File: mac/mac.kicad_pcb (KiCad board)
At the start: 2 copper layers, 70 x 45 mm, 87 parts, among them M3 Отверстие_М3

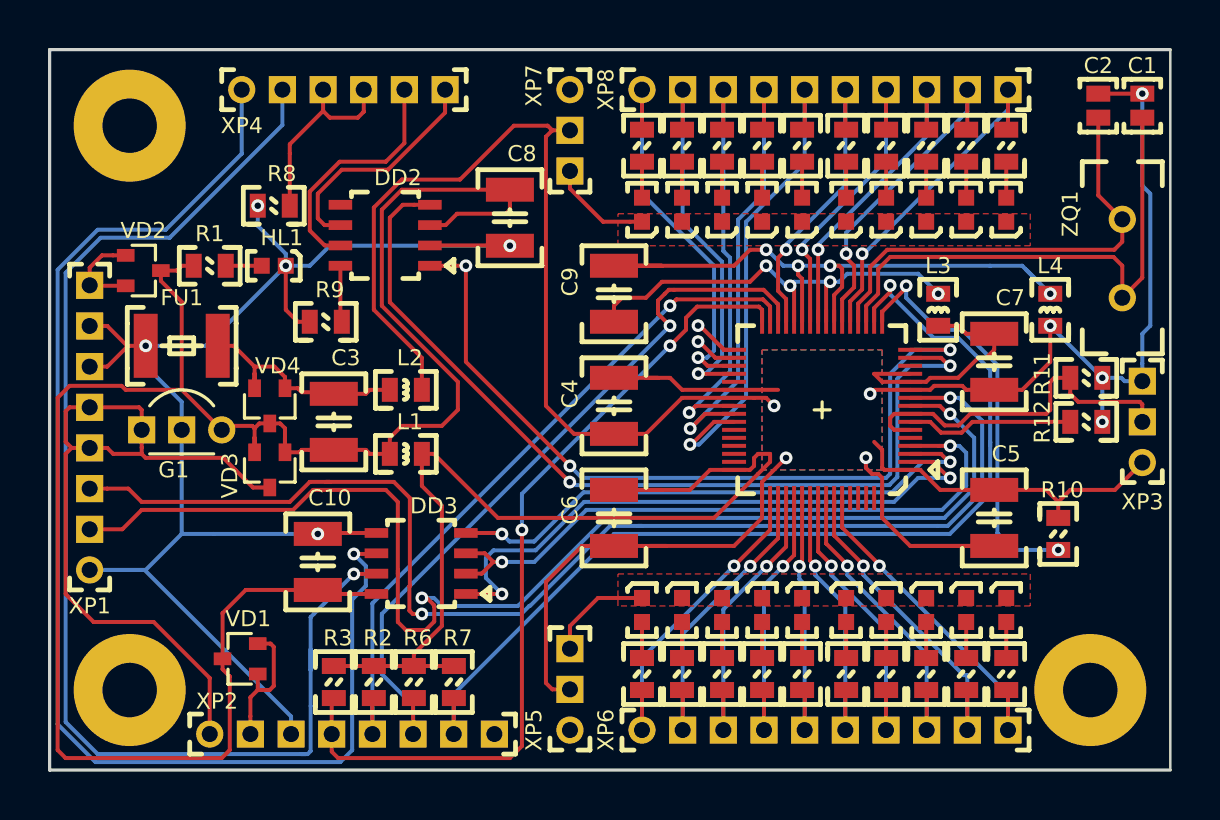
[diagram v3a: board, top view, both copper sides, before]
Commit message: причесывание
-изменен габарит: 72х47 мм
-добавлены заливки земли на обратной стороне
-переходные отверстия вынесены за пределы контактных площадок
-прототип рекламки шелкографией
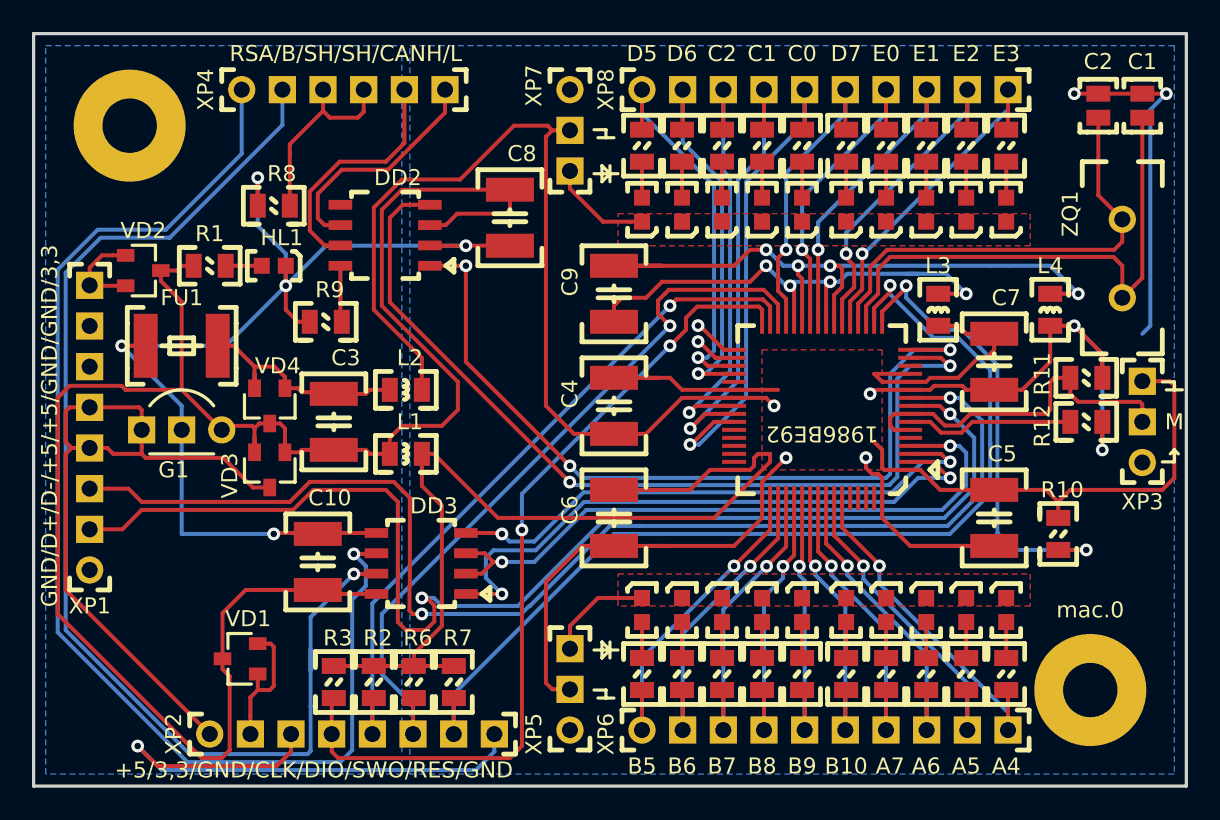
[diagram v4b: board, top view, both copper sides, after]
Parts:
- removed the M3 at (82.5, 97.5)
- moved G*** 4.80 mm to (113.5, 71.5)
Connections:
- XP2 pad 8: Net-(XP2-Pad8) -> /GND
- XP3 pad 1: /VCC_MC -> /GND_MC
- XP3 pad 3: /GND_MC -> /VCC_MC
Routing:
- net /GND: track 95.2 -> 105.9 mm, vias 5 -> 6
- net /VCC_MC: track 106.9 -> 116.3 mm
- net /GND_MC: track 151.8 -> 157.9 mm
- net /VCC: track 126.5 -> 121.5 mm
- net /A_VCC_MC: track 28.6 -> 32.8 mm
- net Net-(DD1-Pad17): track 25.8 -> 29.3 mm
- net /RS_B: track 79.0 -> 75.7 mm
- net /RS_A: track 81.7 -> 78.3 mm
- net /+4...30: track 47.5 -> 45.3 mm
- net /A_GND_MC: track 42.2 -> 44.3 mm
- added copper zone on B.Cu, net /GND
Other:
- board size 70 x 45 mm -> 72 x 47 mm
- board text added: "+5/3,3/GND/CLK/DIO/SWO/RES/GND"
- board text added: "- Разработка (PCB-design) - Опытное изготовление - Мелкосерийный монтаж печатных плат"
- board text added: "1986ВЕ92"
- board text added: "A4"
- board text added: "A5"
- board text added: "A6"
- board text added: "A7"
- board text added: "B10"
- board text added: "B5"
- board text added: "B6"
- board text added: "B7"
- board text added: "B8"
- board text added: "B9"
- board text added: "C0"
- board text added: "C1"
- board text added: "C2"
- board text added: "D5"
- board text added: "D6"
- board text added: "D7"
- board text added: "E0"
- board text added: "E1"
- board text added: "E2"
- board text added: "E3"
- board text added: "El.Nikitos@mail.ru +7(999)123-45-67 WhatsApp, Viber"
- board text added: "GND/D+/D-/+5/+5/GND/GND/3,3"
- board text added: "M"
- board text added: "RSA/B/SH/SH/CANH/L"

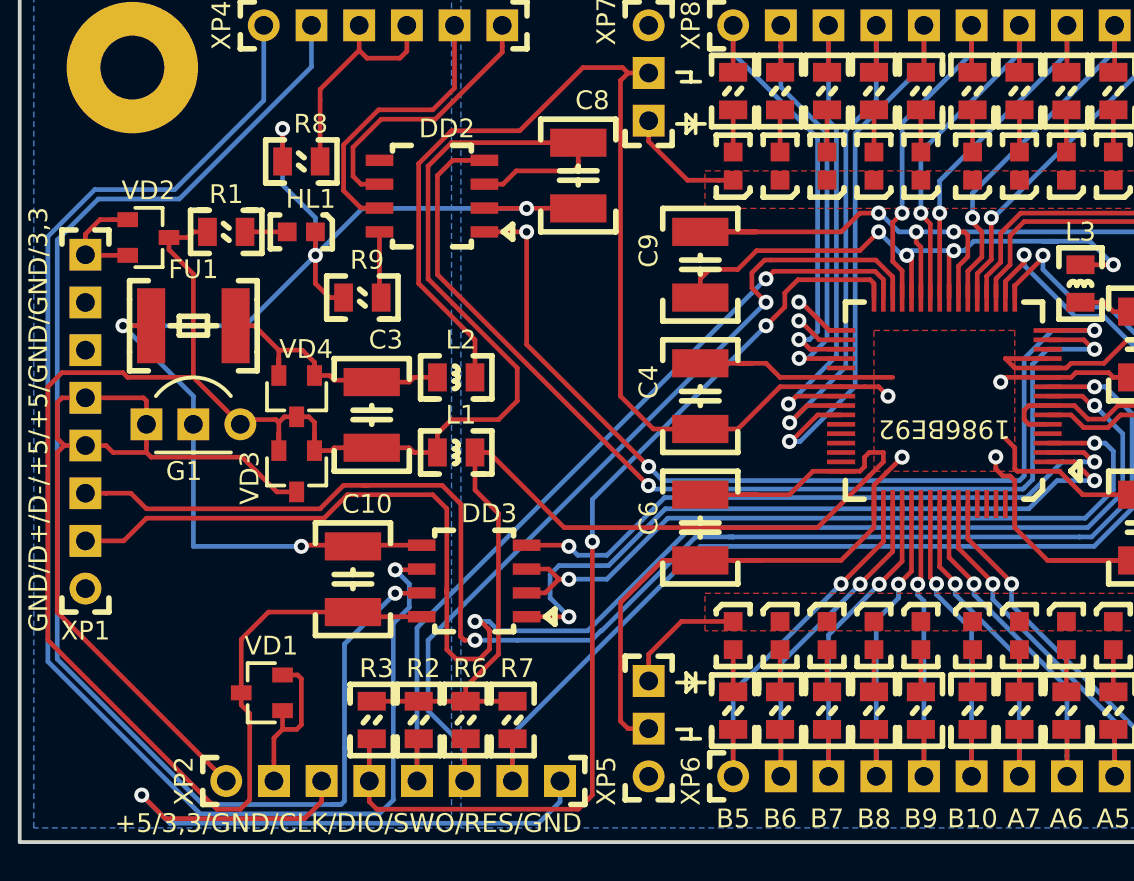
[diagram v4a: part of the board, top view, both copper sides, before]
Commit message: добавлен номер телефона, исправлено положение стабилизатора
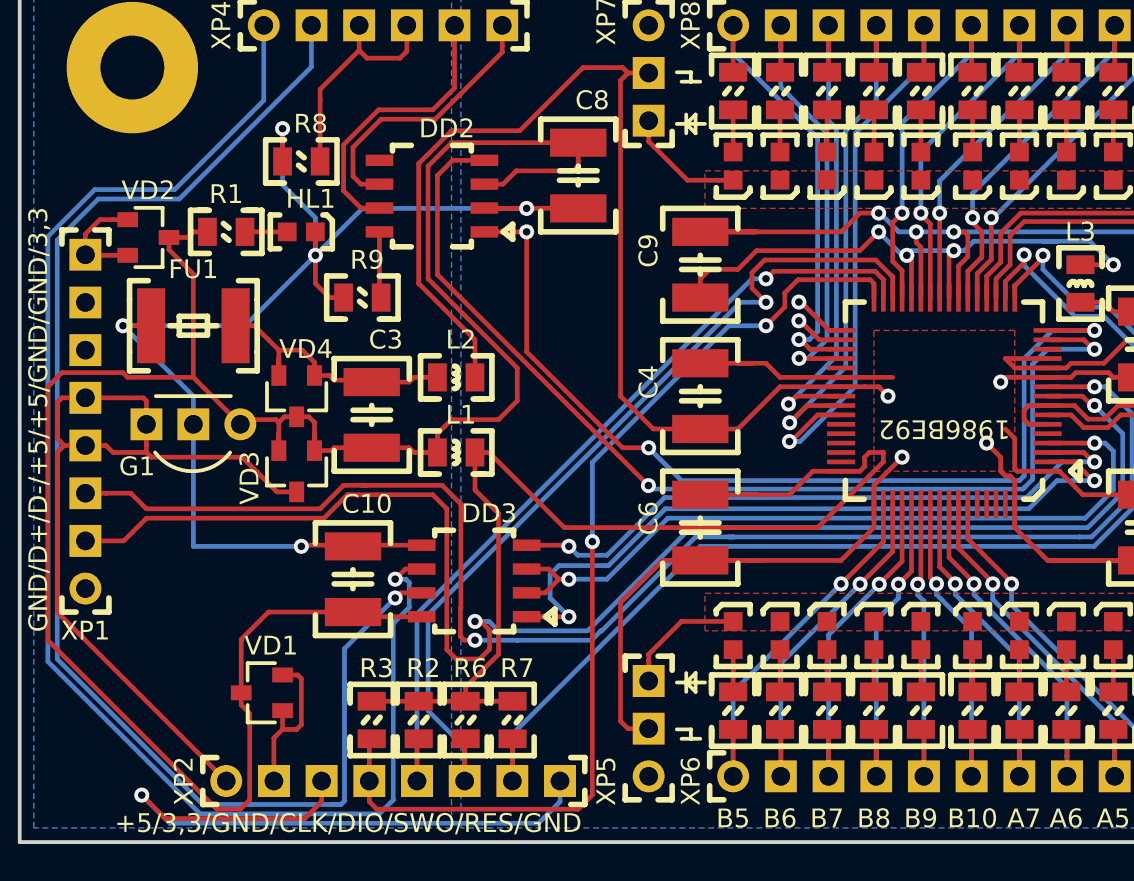
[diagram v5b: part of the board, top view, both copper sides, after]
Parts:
- moved G*** 3.02 mm to (112.2, 68.8)
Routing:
- net /TCK_CLK_TX: track 52.6 -> 53.8 mm
- net /GND_MC: track 157.9 -> 158.7 mm
- net /TDO_SWO: track 47.2 -> 48.0 mm
- net /VCC_MC: track 116.3 -> 116.8 mm
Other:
- board text added: "-разработка (PCB-design) -опытное производство -подготовка к серийному производству -мелкосерийный монтаж -импортозамещение ( если надо :)"
- board text added: "El.Nikitos@mail.ru / El.A.Nikitos@gmail.com +7(995)120-05-23 WhatsApp, Viber"
- board text added: "Печатные платы:"
- board text removed: "- Разработка (PCB-design) - Опытное изготовление - Мелкосерийный монтаж печатных плат"
- board text removed: "El.Nikitos@mail.ru +7(999)123-45-67 WhatsApp, Viber"

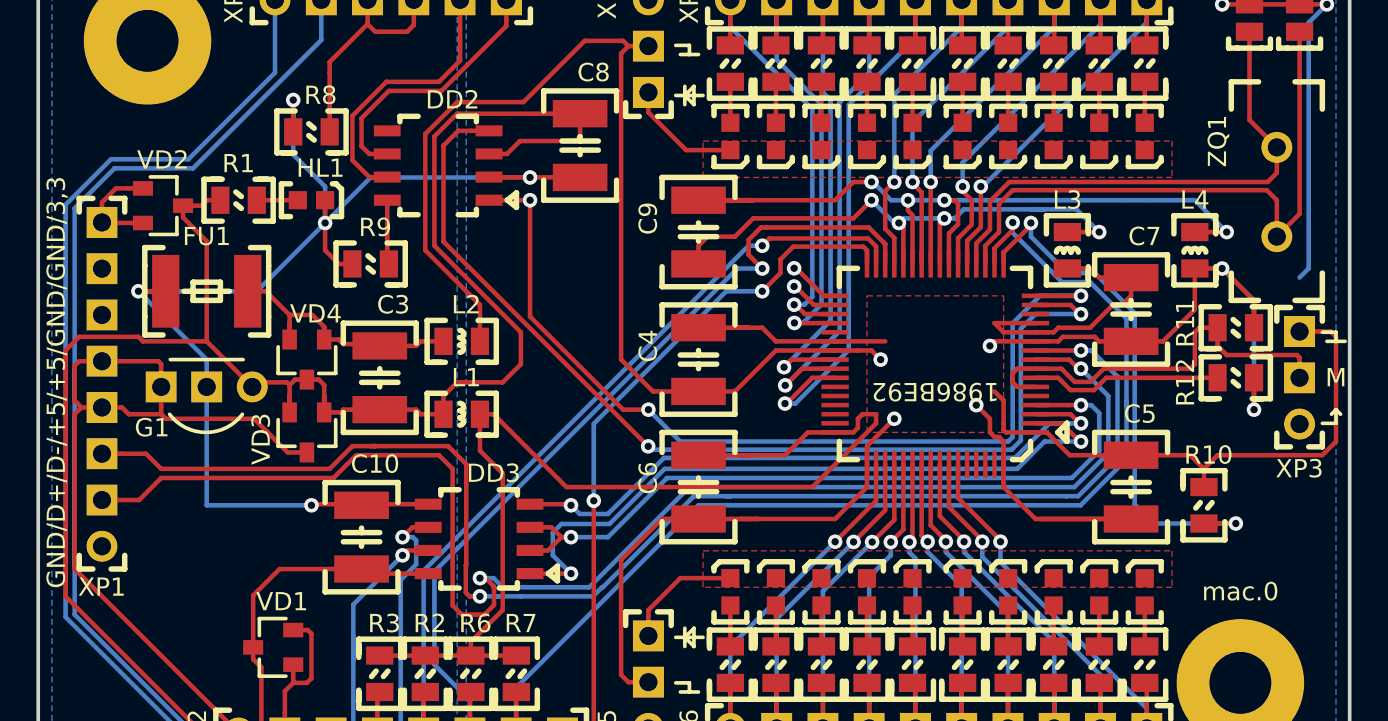
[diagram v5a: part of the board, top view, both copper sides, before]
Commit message: откорректирована надпись, перенесен id + добавлены gerber-файлы
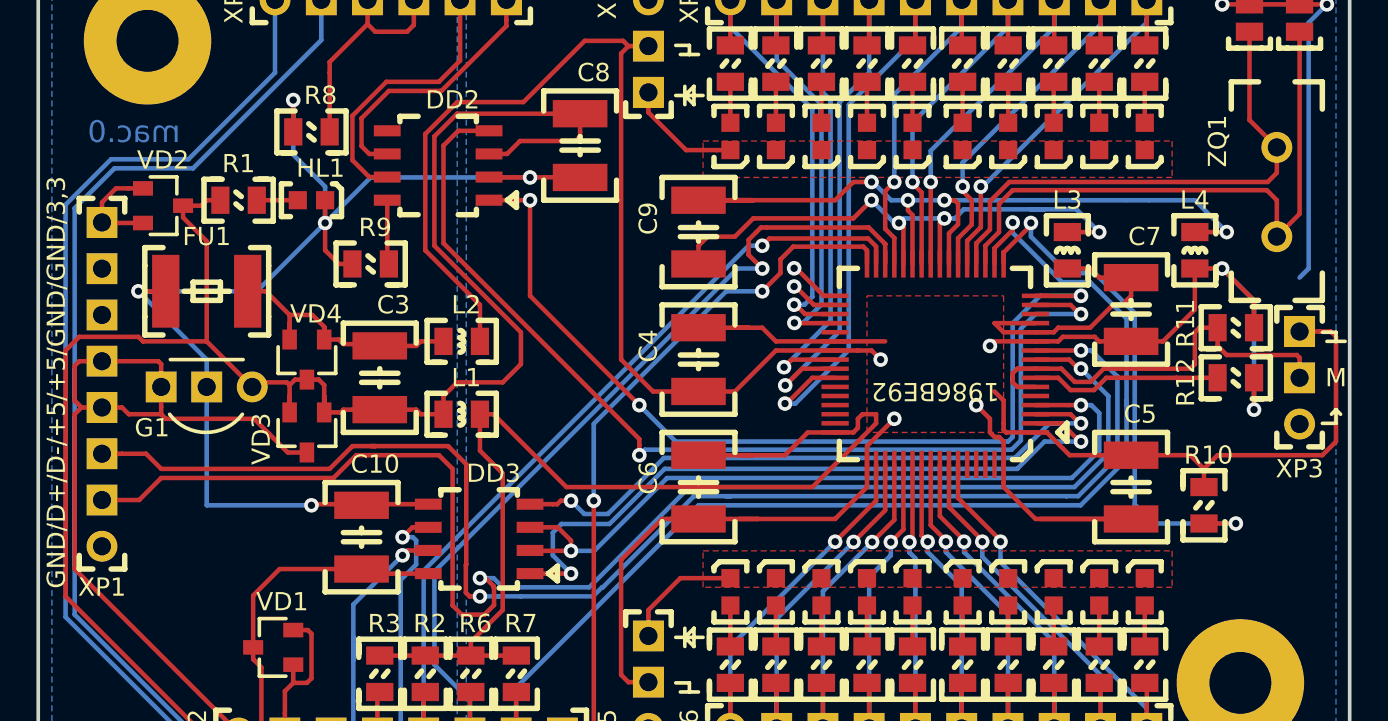
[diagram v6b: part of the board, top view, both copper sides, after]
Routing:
- net /PF2_U2-En: track 41.2 -> 42.4 mm
- net /PE6_C2-TX: track 57.2 -> 58.1 mm
- net /PE6_C2-RX: track 51.2 -> 50.5 mm
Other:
- rule pad_to_mask_clearance: 0.2 -> 0.05
- board text added: "-разработка (PCB-design) -опытное производство -документация по ЕСКД -мелкосерийный монтаж -импортозамещение ( если надо :)"
- board text removed: "-разработка (PCB-design) -опытное производство -подготовка к серийному производству -мелкосерийный монтаж -импортозамещение ( если надо :)"
